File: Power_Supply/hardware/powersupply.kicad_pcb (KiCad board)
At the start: 2 copper layers, 60.8 x 63.3 mm, 85 parts, among them J1 1x2, J101 USB_B_Micro, J102 Conn_01x03_Male, J103 Default_Jumper, J104 Default_Jumper, J2 1x2, Q1 IRF9Z24NPBF, SW1 KMR2, SW2 joystick-K1-1506DN-01, SW3 KMR2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

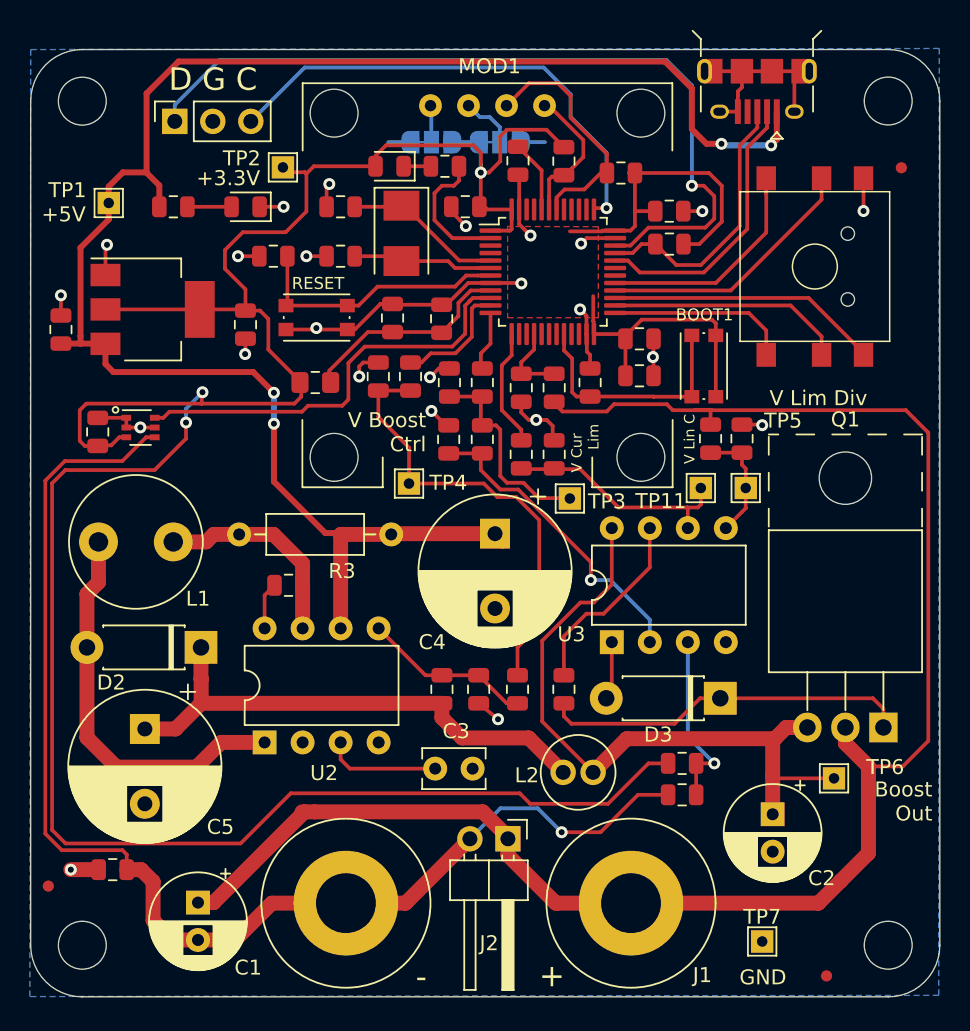
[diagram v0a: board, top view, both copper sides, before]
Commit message: Moved current sense amplifier away from switching components.
Moved current sense amplifier away from switching components.
Moved boost converter filtering components nearer to the output of the
boost converter.
Moved P-MOSFET down a bit so it’s farther away from the joystick.
Firmware: V_current_amplified moved to PB0
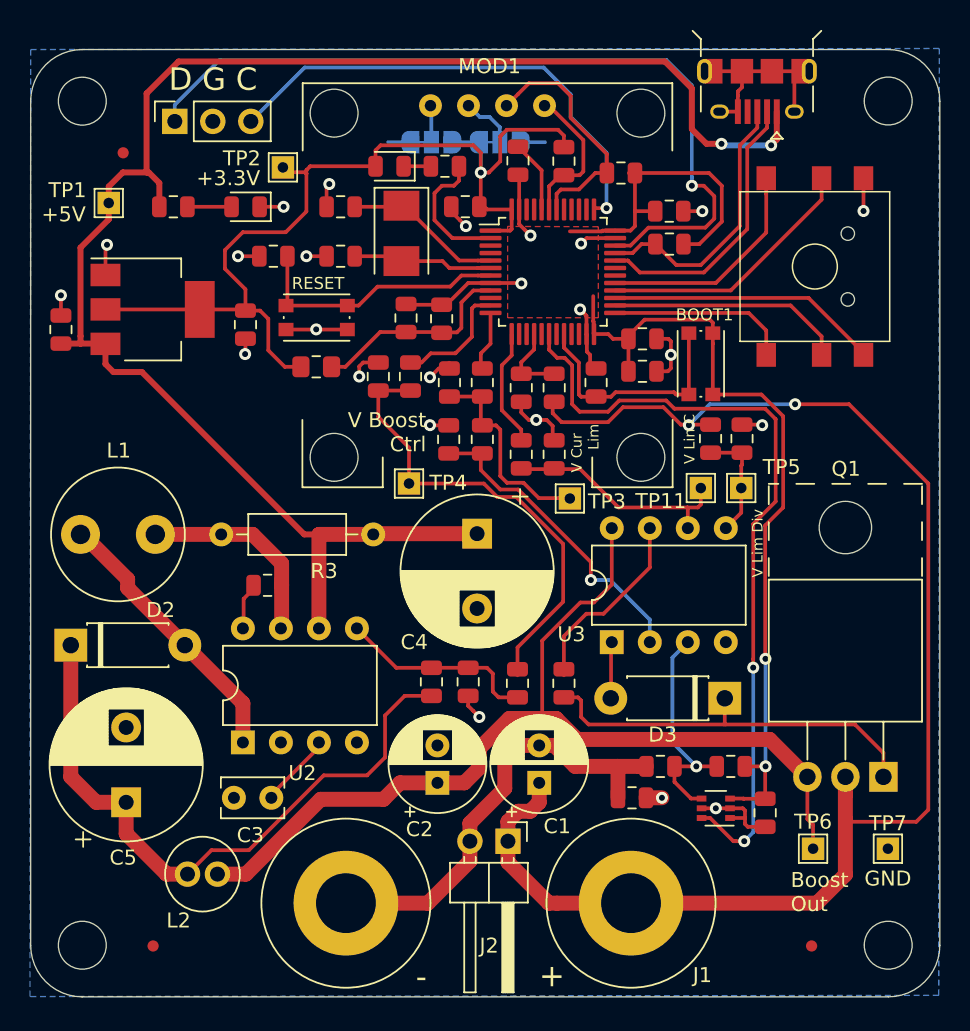
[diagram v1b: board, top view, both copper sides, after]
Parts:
- U102: value INA199 -> INA199A1
- moved TP8 52.0 mm to (35.0, 35.0)
- moved C105 51.4 mm to (77.9, 79.1), turned to 270 degrees
- moved U102 46.1 mm to (74.6, 78.8), turned to 180 degrees
- moved R122 35.0 mm to (69.0, 78.1), turned to 0 degrees
- moved L2 26.0 mm to (40.3, 83.2)
- moved C1 24.2 mm to (62.8, 77.1), turned to 90 degrees
- moved C2 22.5 mm to (56.0, 77.1), turned to 90 degrees
- moved C3 11.1 mm to (44.9, 78.1), turned to 180 degrees
- moved TP7 10.4 mm to (86.1, 81.5)
- moved D2 8.70 mm to (31.5, 67.9), turned to 0 degrees
- moved TP9 8.06 mm to (37.0, 88.0)
- moved C5 5.06 mm to (35.2, 78.4), turned to 90 degrees
- moved TP6 4.90 mm to (81.1, 81.5)
- moved Q1 3.30 mm to (85.8, 76.7)
- moved R118 3.26 mm to (75.6, 76.0), turned to 180 degrees
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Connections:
- net Net-(R111-Pad1) renamed /V_positive_out_div
- R117 pad 1: Net-(R117-Pad1) -> /V_negative_out_offset
- R118 pad 2: Net-(R117-Pad1) -> /V_negative_out_offset
- U102 pad 4: /V_negative_out -> /V_negative_out_offset
- U103 pad 10: /V_current_amplified -> Net-(U103-Pad10)
- U103 pad 18: Net-(U103-Pad18) -> /V_current_amplified
- U3 pad 3: Net-(R117-Pad1) -> /V_negative_out_offset
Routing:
- net +3V3: track 211.2 -> 143.0 mm
- net /V_negative_out: track 83.6 -> 29.9 mm, vias 1 -> 0
- net /V_current_amplified: track 28.4 -> 52.8 mm, vias 0 -> 2
- net /Boost_out: track 45.0 -> 65.8 mm
- net /V_positive_out: track 115.8 -> 97.1 mm, vias 0 -> 2
- net /V_negative_out_offset: track 0.00 -> 15.7 mm, vias 0 -> 1
- net Net-(R117-Pad1): track 12.1 -> 0.00 mm, vias 1 -> 0
- net Net-(C5-Pad1): track 34.9 -> 43.4 mm
- net Net-(D2-Pad2): track 26.8 -> 18.5 mm
- net +5V: track 118.1 -> 112.2 mm, vias 4 -> 2
- net GND: track 83.0 -> 80.1 mm
- net Net-(R106-Pad2): track 11.4 -> 14.1 mm
- net Net-(C3-Pad1): track 7.71 -> 5.22 mm
- net Net-(D3-Pad1): track 24.7 -> 26.9 mm
- net /V_boost_ctrl: track 29.8 -> 31.1 mm
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
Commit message: Moved label changes to PCB, generated gerbers
Moved label changes to PCB, generated gerbers
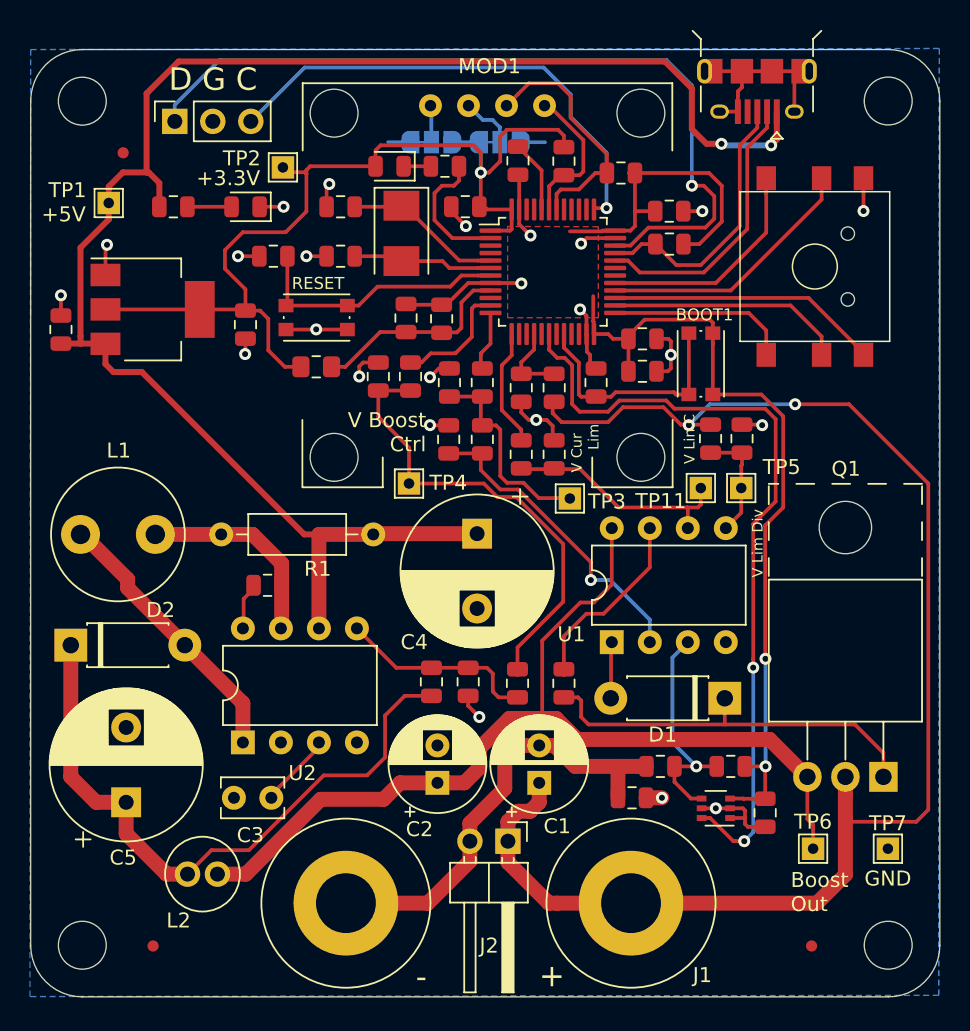
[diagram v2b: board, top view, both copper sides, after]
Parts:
- renumbered D3 to D1, R3 to R1, U3 to U1

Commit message: some layout changes
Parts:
- removed G***: LOGO, powersupply:Logo
- removed R1: 0.3 1/4W, Resistor_THT:R_Axial_DIN0207_L6.3mm_D2.5mm_P10.16mm_Horizontal
- added R126: 0.3 1/4W, Resistor_SMD:R_0805_2012Metric, F.Cu at (44.7, 60.5)
- C116: renamed from C3; footprint Capacitor_THT:C_Rect_L4.0mm_W2.5mm_P2.50mm -> Capacitor_SMD:C_0805_2012Metric
- moved C116 1.21 mm to (43.7, 78.1)
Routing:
- net GND: track 80.1 -> 81.8 mm, vias 24 -> 25
